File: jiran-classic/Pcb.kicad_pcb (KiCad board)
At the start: 2 copper layers, 152.3 x 104.7 mm, 133 parts, among them J1 TRRS, Q1 2N7002, SW1 SW_Push, SW10 SW_Push, SW11 SW_Push, SW12 SW_Push, SW13 SW_Push, SW14 SW_Push, SW15 SW_Push, SW16 SW_Push, SW17 SW_Push, SW18 SW_Push, SW19 SW_Push, SW2 SW_Push, SW20 SW_Push, SW21 SW_Push, SW22 SW_Push, SW23 SW_Push, SW24 SW_Push, SW25 SW_Push, SW26 SW_Push, SW27 SW_Push, SW28 SW_Push, SW29 SW_Push, SW3 SW_Push, SW4 SW_Push, SW5 SW_Push, SW6 SW_Push, SW7 SW_Push, SW8 SW_Push, SW9 SW_Push, U1 ProMicro

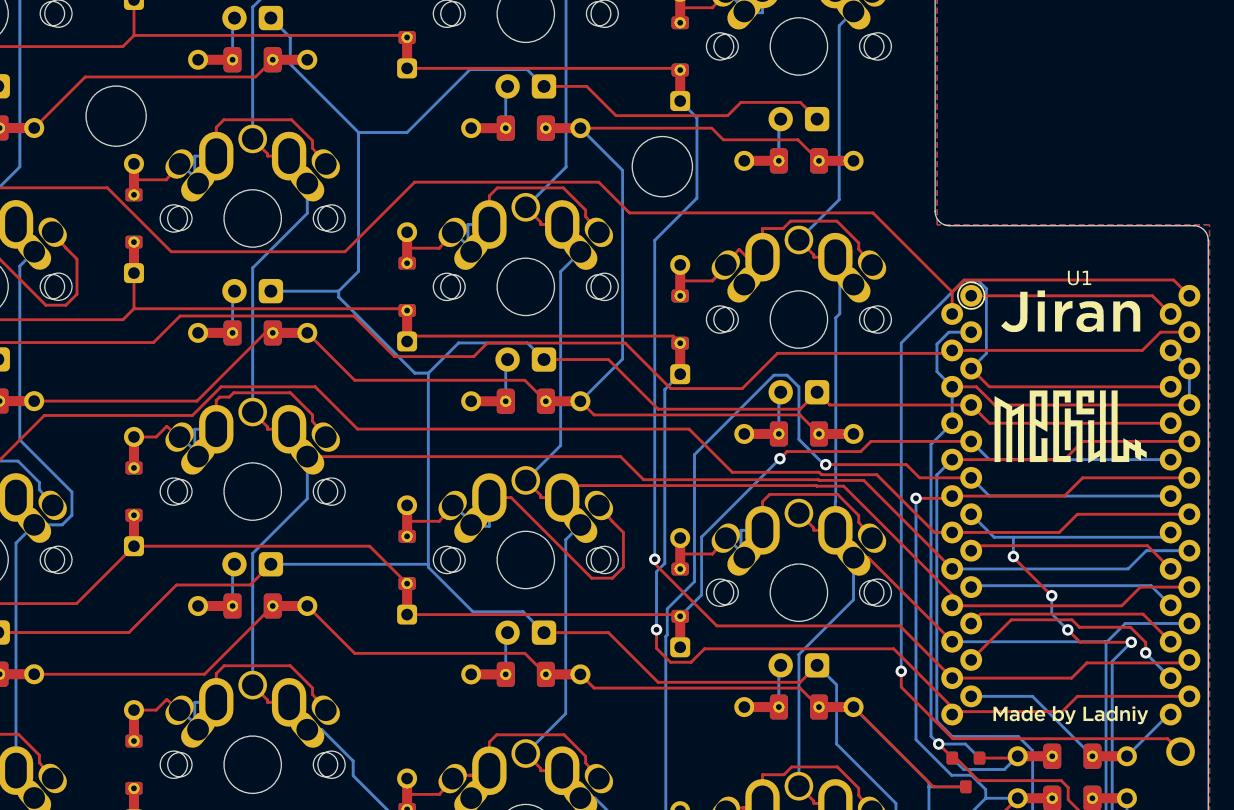
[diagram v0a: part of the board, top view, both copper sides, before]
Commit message: Remove one hole mount (HM3)
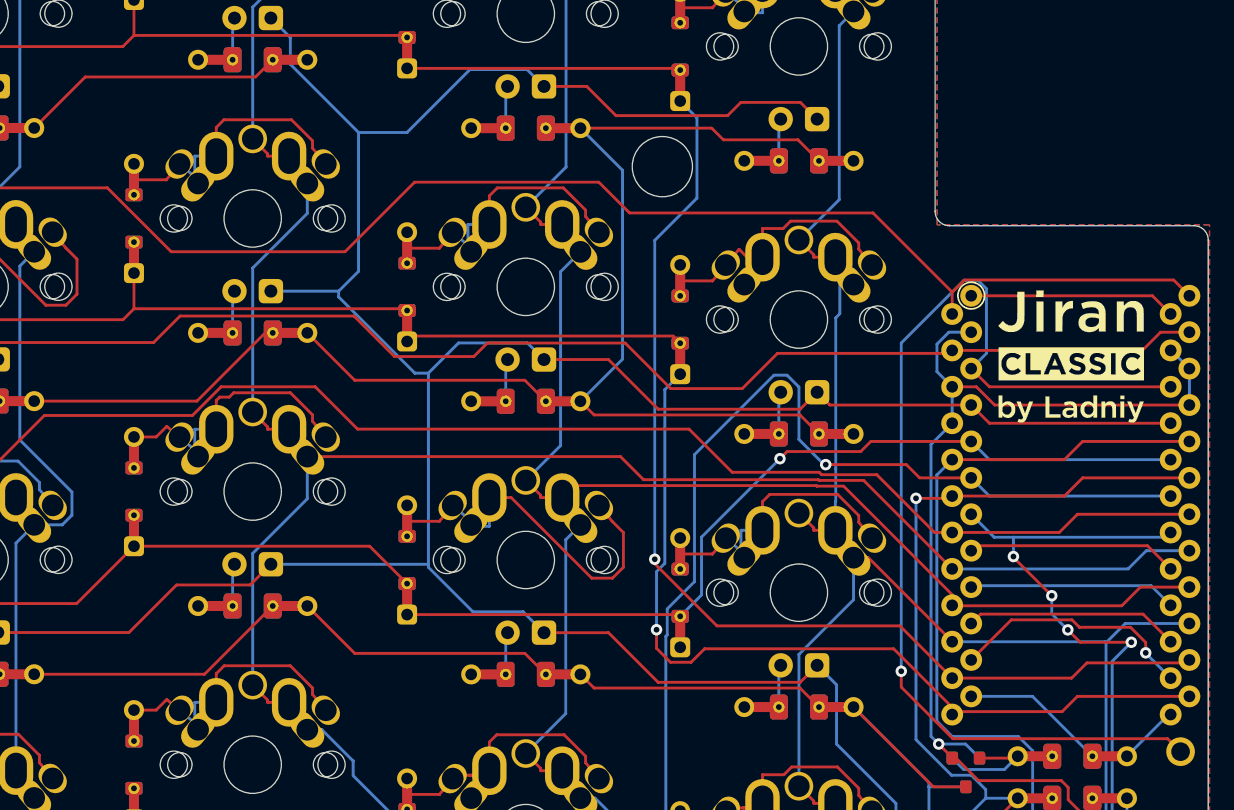
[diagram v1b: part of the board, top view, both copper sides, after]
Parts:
- removed the HM3 at (153.3, 51.5)
- removed LG1, LG2: Silk_Logo_New, Used_Footprints:Silk_Logo_New
- added G1: LOGO, used_footprints:Silk_Logotype, F.Cu at (219.9, 77.2)
- added G2: LOGO, used_footprints:Silk_Logotype, B.Cu at (219.9, 77.2)
- renumbered HM4 to HM3, HM5 to HM4, HM6 to HM5
